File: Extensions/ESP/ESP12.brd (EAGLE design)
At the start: 65 x 30 mm, 8 parts, among them IC1 REG1117, J1 RASPBERRYPI-40-PIN-GPIO_PTH_N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

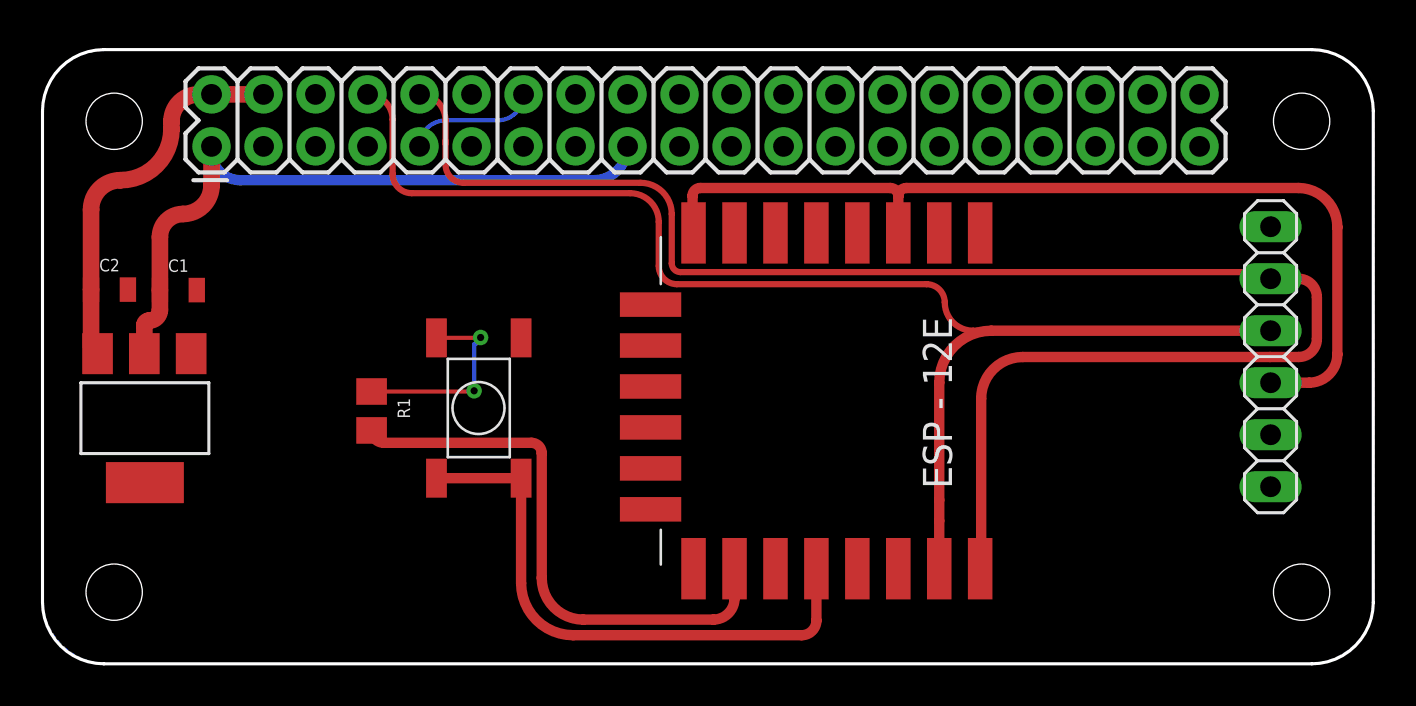
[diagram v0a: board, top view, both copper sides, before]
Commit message: Updated ESP expansion; now teledildonics and swapped TX and RX lines
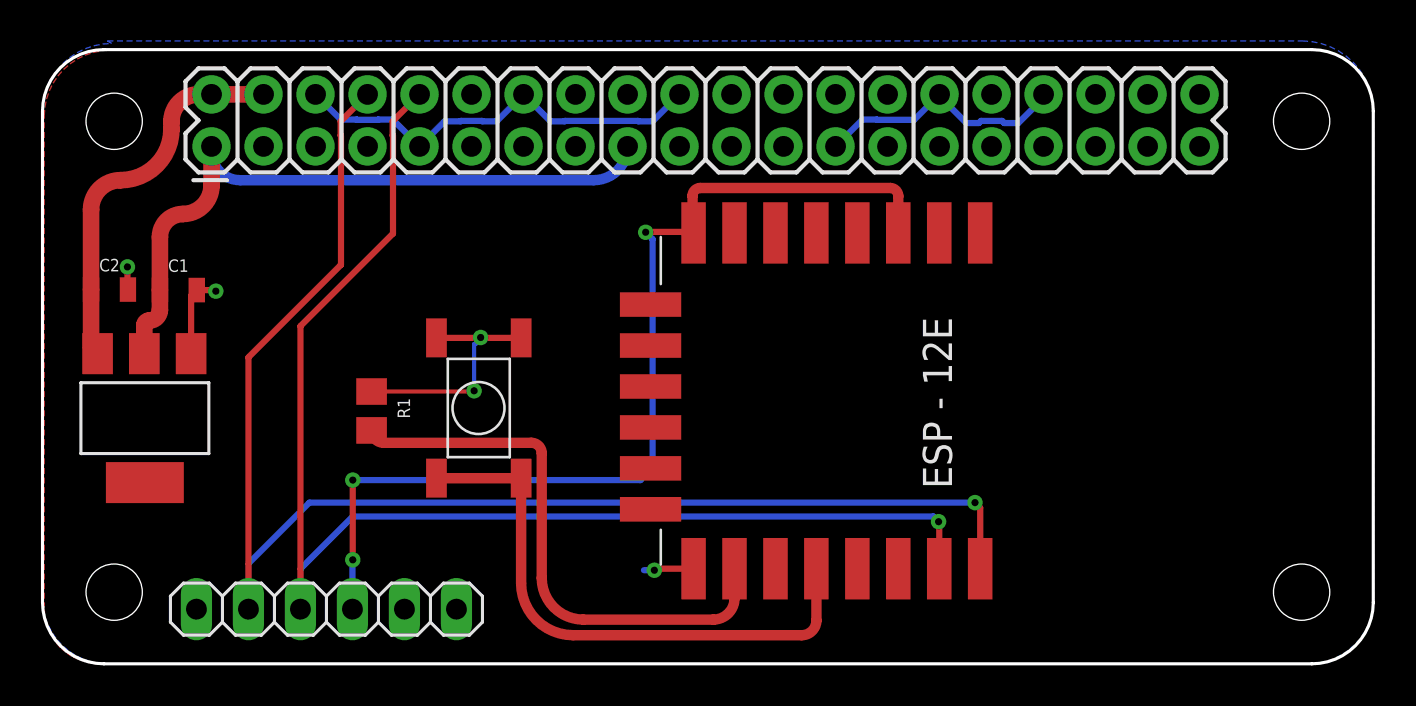
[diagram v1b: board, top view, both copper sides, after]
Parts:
- moved JP2 47.7 mm to (13.9, 2.67), turned to 180 degrees
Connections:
- net FTDI_RX: now also J1.8; no longer J1.10
- net FTDI_TX: now also J1.10; no longer J1.8
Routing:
- net GND: track 16.1 -> 55.4 mm, vias 2 -> 5
- net FTDI_RX: track 78.7 -> 69.8 mm, vias 0 -> 1
- net 3V3: track 46.5 -> 49.2 mm, vias 0 -> 3
- net FTDI_TX: track 64.4 -> 64.2 mm, vias 0 -> 1
- added copper zone on layer 1, net VCC
- removed copper zone on layer 1, net GND

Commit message: escape code handling
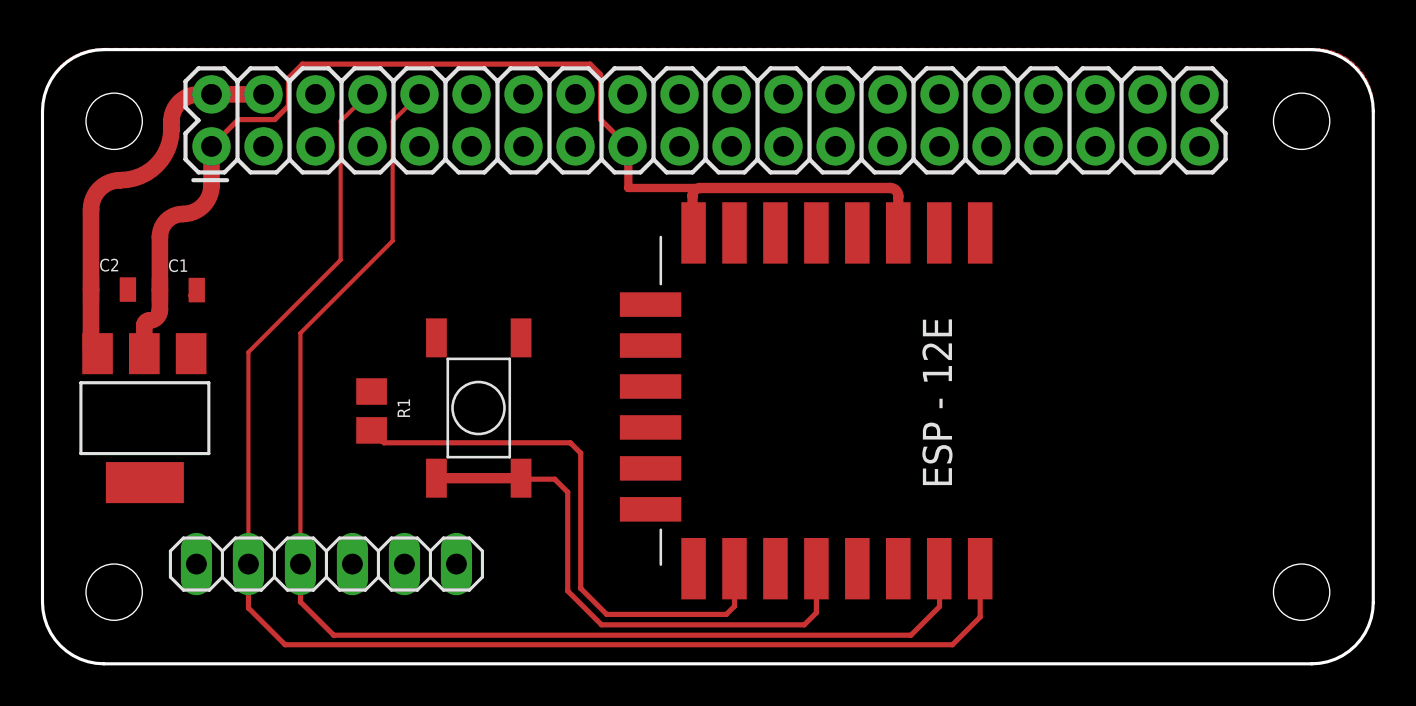
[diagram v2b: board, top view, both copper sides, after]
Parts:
- moved JP2 2.20 mm to (13.9, 4.87)
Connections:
- net 3V3: no longer U3.CH_PD, U3.VCC
- net VCC: now also U3.CH_PD, U3.VCC
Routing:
- net GND: track 55.4 -> 0.42 mm, vias 5 -> 0
- net 3V3: track 49.2 -> 0.00 mm, vias 3 -> 0
- net VCC: track 33.3 -> 57.0 mm
- net FTDI_RX: track 69.8 -> 66.9 mm, vias 1 -> 0
- net FTDI_TX: track 64.2 -> 61.5 mm, vias 1 -> 0
- added copper zone on layer 1, net GND
- removed copper zone on layer 16, net GND
- removed copper zone on layer 1, net VCC
